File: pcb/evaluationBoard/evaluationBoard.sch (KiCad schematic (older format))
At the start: 0 parts

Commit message: power schematic completed
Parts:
- added IC1: STM32F429ZGT6, QFP50P2200X2200X160-144N, symbol MCU_JLC:STM32F429ZGT6
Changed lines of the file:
@@
 $Descr A3 16535 11693
 encoding utf-8
-Sheet 1 1
+Sheet 1 3
 Title "Evaluation Board"
 Date "2021-01-07"
@@
 Comment4 ""
 $EndDescr
+$Comp
+L MCU_JLC:STM32F429ZGT6 IC1
+U 1 1 5FF751EB
+P 6100 3500
+F 0 "IC1" H 10244 1796 50  0000 L CNN
+F 1 "STM32F429ZGT6" H 10244 1705 50  0000 L CNN
+F 2 "QFP50P2200X2200X160-144N" H 10050 4000 50  0001 L CNN
+F 3 "http://www.st.com/web/en/resource/technical/document/datasheet/DM00071990.pdf" H 10050 3900 50  0001 L CNN
+F 4 "32-Bit MCU+FPU M4 1MB LCD-TFT LQFP144 STMicroelectronics STM32F429ZGT6, 32bit ARM Cortex M4 MCU, 180MHz, 1024 kB Flash, 144-Pin LQFP" H 10050 3800 50  0001 L CNN "Description"
+F 5 "1.6" H 10050 3700 50  0001 L CNN "Height"
+F 6 "511-STM32F429ZGT6" H 10050 3600 50  0001 L CNN "Mouser Part Number"
+F 7 "https://www.mouser.co.uk/ProductDetail/STMicroelectronics/STM32F429ZGT6?qs=DqCdCwOw4%2F61O51evUvYMQ%3D%3D" H 10050 3500 50  0001 L CNN "Mouser Price/Stock"
+F 8 "STMicroelectronics" H 10050 3400 50  0001 L CNN "Manufacturer_Name"
+F 9 "STM32F429ZGT6" H 10050 3300 50  0001 L CNN "Manufacturer_Part_Number"
+F 10 "C46525" H 6100 3500 50  0001 C CNN "LCSC"
+	1    6100 3500
+	1    0    0    -1
+$EndComp
+$Sheet
+S 3250 2650 1050 800
+U 5FF87377
+F0 "power" 50
+F1 "power.sch" 50
+F2 "ENA" I R 4300 2750 50
+$EndSheet
+$Sheet
+S 3250 3650 1050 550
+U 5FFF84E6
+F0 "dsp" 50
+F1 "dsp.sch" 50
+$EndSheet
 $EndSCHEMATC

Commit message: updated design
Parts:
- removed IC1: STM32F429ZGT6, QFP50P2200X2200X160-144N, symbol MCU_JLC:STM32F429ZGT6
- added IC?: STM32F429ZGT6, QFP50P2200X2200X160-144N, symbol MCU_JLC:STM32F429ZGT6
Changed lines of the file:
@@
 Sheet 1 3
 Title "Evaluation Board"
-Date "2021-01-07"
+Date "2021-01-11"
 Rev "A"
 Comp "Jason Too"
@@
 Comment4 ""
 $EndDescr
-$Comp
-L MCU_JLC:STM32F429ZGT6 IC1
-U 1 1 5FF751EB
-P 6100 3500
-F 0 "IC1" H 10244 1796 50  0000 L CNN
-F 1 "STM32F429ZGT6" H 10244 1705 50  0000 L CNN
-F 2 "QFP50P2200X2200X160-144N" H 10050 4000 50  0001 L CNN
-F 3 "http://www.st.com/web/en/resource/technical/document/datasheet/DM00071990.pdf" H 10050 3900 50  0001 L CNN
-F 4 "32-Bit MCU+FPU M4 1MB LCD-TFT LQFP144 STMicroelectronics STM32F429ZGT6, 32bit ARM Cortex M4 MCU, 180MHz, 1024 kB Flash, 144-Pin LQFP" H 10050 3800 50  0001 L CNN "Description"
-F 5 "1.6" H 10050 3700 50  0001 L CNN "Height"
-F 6 "511-STM32F429ZGT6" H 10050 3600 50  0001 L CNN "Mouser Part Number"
-F 7 "https://www.mouser.co.uk/ProductDetail/STMicroelectronics/STM32F429ZGT6?qs=DqCdCwOw4%2F61O51evUvYMQ%3D%3D" H 10050 3500 50  0001 L CNN "Mouser Price/Stock"
-F 8 "STMicroelectronics" H 10050 3400 50  0001 L CNN "Manufacturer_Name"
-F 9 "STM32F429ZGT6" H 10050 3300 50  0001 L CNN "Manufacturer_Part_Number"
-F 10 "C46525" H 6100 3500 50  0001 C CNN "LCSC"
-	1    6100 3500
-	1    0    0    -1
-$EndComp
 $Sheet
-S 3250 2650 1050 800
-U 5FF87377
-F0 "power" 50
-F1 "power.sch" 50
-F2 "ENA" I R 4300 2750 50
-$EndSheet
-$Sheet
-S 3250 3650 1050 550
-U 5FFF84E6
+S 4100 3350 950  450
+U 5FFC8352
 F0 "dsp" 50
 F1 "dsp.sch" 50
 $EndSheet
+$Sheet
+S 4100 4650 1000 650
+U 5FFC85D7
+F0 "power" 50
+F1 "power.sch" 50
+$EndSheet
+$Comp
+L MCU_JLC:STM32F429ZGT6 IC?
+U 1 1 5FFCAABC
+P 6700 3200
+F 0 "IC?" H 10844 1496 50  0000 L CNN
+F 1 "STM32F429ZGT6" H 10844 1405 50  0000 L CNN
+F 2 "QFP50P2200X2200X160-144N" H 10650 3700 50  0001 L CNN
+F 3 "http://www.st.com/web/en/resource/technical/document/datasheet/DM00071990.pdf" H 10650 3600 50  0001 L CNN
+F 4 "32-Bit MCU+FPU M4 1MB LCD-TFT LQFP144 STMicroelectronics STM32F429ZGT6, 32bit ARM Cortex M4 MCU, 180MHz, 1024 kB Flash, 144-Pin LQFP" H 10650 3500 50  0001 L CNN "Description"
+F 5 "1.6" H 10650 3400 50  0001 L CNN "Height"
+F 6 "511-STM32F429ZGT6" H 10650 3300 50  0001 L CNN "Mouser Part Number"
+F 7 "https://www.mouser.co.uk/ProductDetail/STMicroelectronics/STM32F429ZGT6?qs=DqCdCwOw4%2F61O51evUvYMQ%3D%3D" H 10650 3200 50  0001 L CNN "Mouser Price/Stock"
+F 8 "STMicroelectronics" H 10650 3100 50  0001 L CNN "Manufacturer_Name"
+F 9 "STM32F429ZGT6" H 10650 3000 50  0001 L CNN "Manufacturer_Part_Number"
+F 10 "C46525" H 6700 3200 50  0001 C CNN "LCSC"
+	1    6700 3200
+	1    0    0    -1
+$EndComp
 $EndSCHEMATC

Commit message: wip
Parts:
- gave numbers to parts that had none: 1
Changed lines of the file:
@@
 $Descr A3 16535 11693
 encoding utf-8
-Sheet 1 3
+Sheet 1 4
 Title "Evaluation Board"
 Date "2021-01-11"
@@
 $EndDescr
 $Sheet
-S 4100 3350 950  450
+S 4200 4200 750  1500
 U 5FFC8352
 F0 "dsp" 50
 F1 "dsp.sch" 50
+F2 "~RESET" I R 4950 4300 50
+F3 "GPIO" I R 4950 4400 50
+F4 "MISO" I R 4950 4500 50
+F5 "SDA" I R 4950 4600 50
+F6 "SCL" I R 4950 4700 50
+F7 "DOUT" I R 4950 4800 50
+F8 "DIN" I R 4950 4900 50
+F9 "WCLK" I R 4950 5000 50
+F10 "BCLK" I R 4950 5100 50
+F11 "MCLK" I R 4950 5200 50
+F12 "MIC+" I L 4200 5600 50
+F13 "MIC-" I L 4200 5500 50
+F14 "LOL" I L 4200 5300 50
+F15 "-LOR" I L 4200 4400 50
+F16 "LOR" I L 4200 5400 50
+F17 "-IN2_R" I L 4200 4900 50
+F18 "-IN2_L" I L 4200 4800 50
+F19 "-IN1_L" I L 4200 5050 50
+F20 "-IN1_R" I L 4200 5150 50
+F21 "-HPL" I L 4200 4550 50
+F22 "-HPR" I L 4200 4650 50
+F23 "-LOL" I L 4200 4300 50
 $EndSheet
 $Sheet
-S 4100 4650 1000 650
+S 4200 5900 750  200
 U 5FFC85D7
 F0 "power" 50
 F1 "power.sch" 50
+F2 "ENA" I R 4950 6000 50
 $EndSheet
 $Comp
-L MCU_JLC:STM32F429ZGT6 IC?
+L MCU_JLC:STM32F429ZGT6 IC1
 U 1 1 5FFCAABC
 P 6700 3200
-F 0 "IC?" H 10844 1496 50  0000 L CNN
+F 0 "IC1" H 10844 1496 50  0000 L CNN
 F 1 "STM32F429ZGT6" H 10844 1405 50  0000 L CNN
 F 2 "QFP50P2200X2200X160-144N" H 10650 3700 50  0001 L CNN
@@
 	1    0    0    -1
 $EndComp
+$Sheet
+S 4150 6400 800  400
+U 6059D58E
+F0 "GPS" 50
+F1 "GPS.sch" 50
+$EndSheet
+$Sheet
+S 4150 7050 550  500
+U 6059D6D4
+F0 "sensors" 50
+F1 "sensors.sch" 50
+$EndSheet
 $EndSCHEMATC

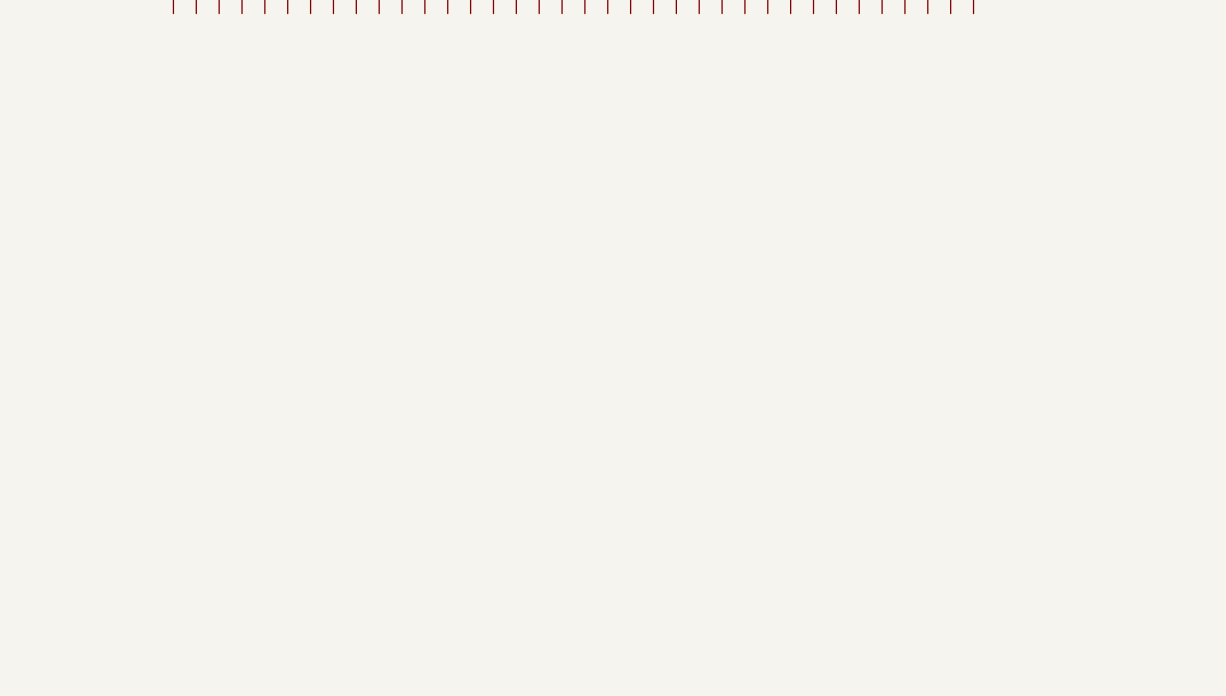
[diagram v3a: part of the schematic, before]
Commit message: added modules
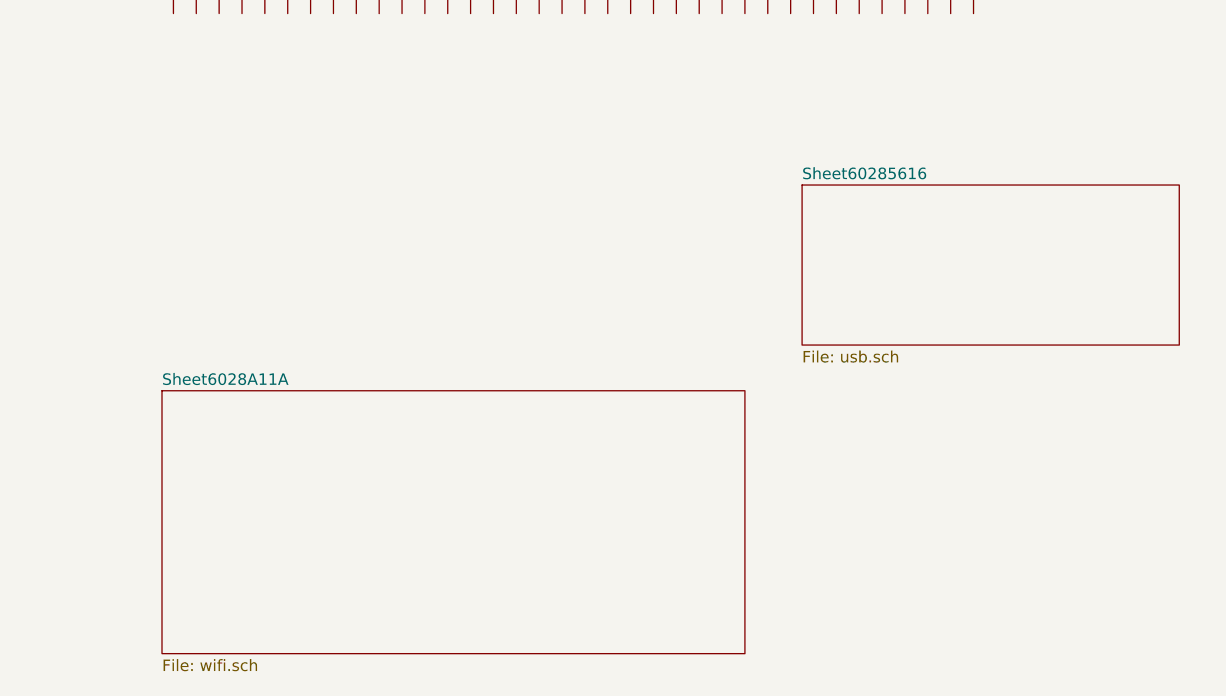
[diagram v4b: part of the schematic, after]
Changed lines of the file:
@@
 $Descr A3 16535 11693
 encoding utf-8
-Sheet 1 4
+Sheet 1 7
 Title "Evaluation Board"
 Date "2021-01-11"
@@
 F1 "sensors.sch" 50
 $EndSheet
+$Sheet
+S 9750 8150 1650 700
+U 60285617
+F0 "Sheet60285616" 50
+F1 "usb.sch" 50
+$EndSheet
+$Sheet
+S 6950 9050 2550 1150
+U 6028A11B
+F0 "Sheet6028A11A" 50
+F1 "wifi.sch" 50
+$EndSheet
 $EndSCHEMATC
